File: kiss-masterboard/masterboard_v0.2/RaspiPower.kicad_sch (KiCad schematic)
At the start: 14 parts, among them U1 TPS54327

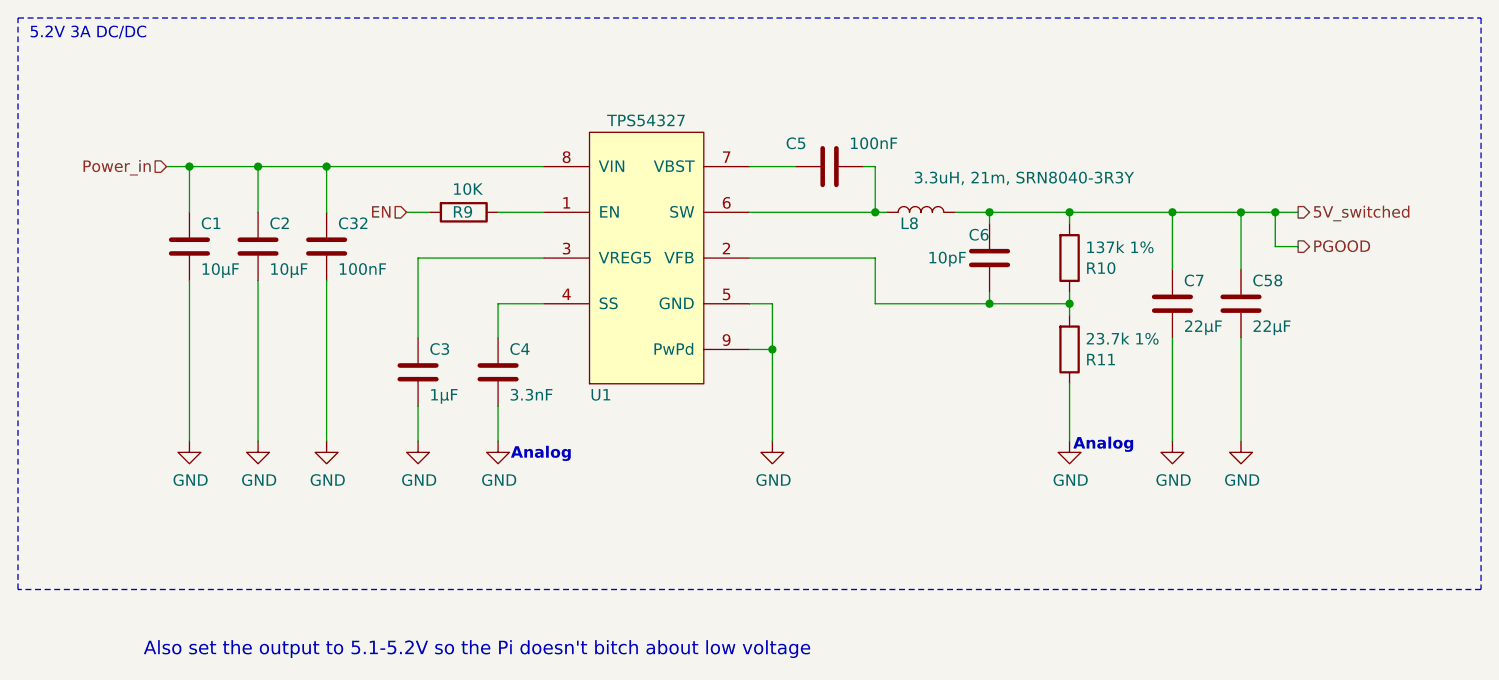
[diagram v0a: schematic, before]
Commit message: Replaced TPS54327 with TPS56339DDC and adjusted the schematic layout accordingly.
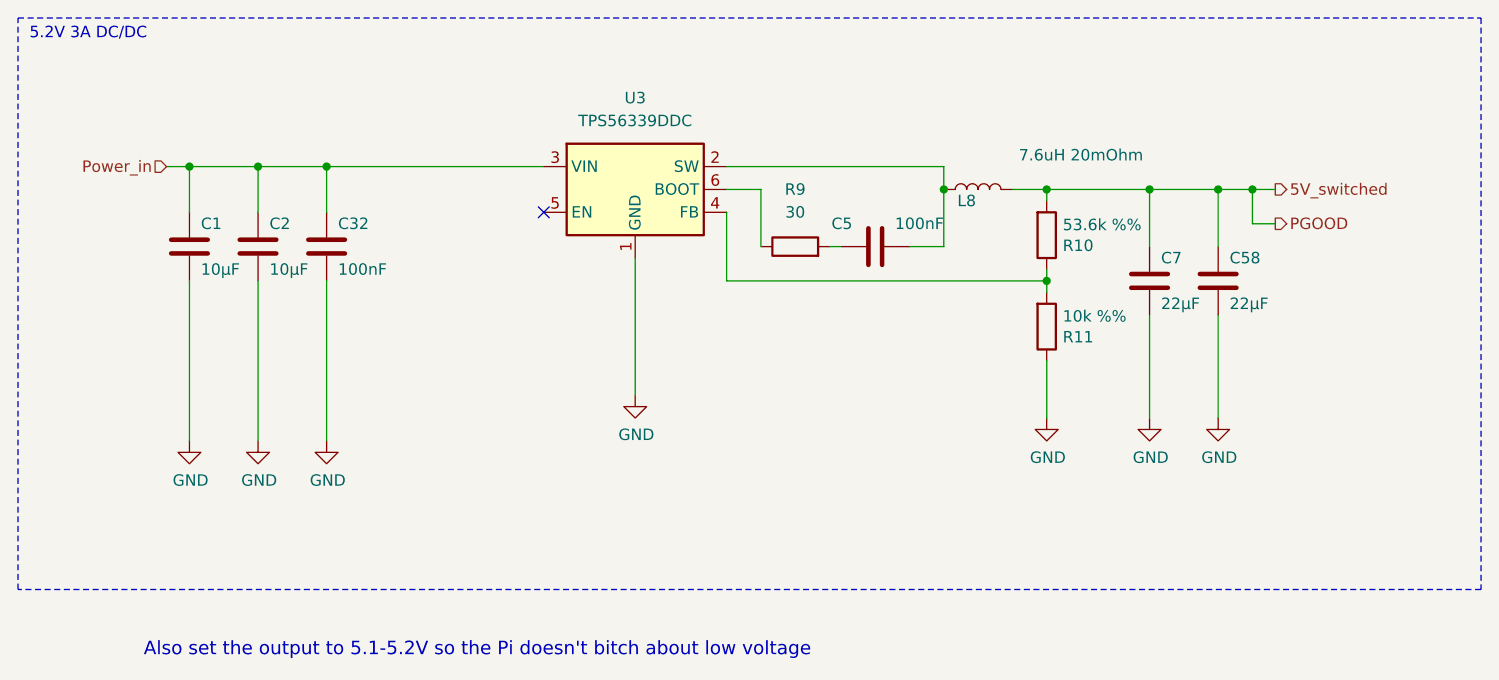
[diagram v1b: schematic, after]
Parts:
- removed C3: 1µF, Capacitor_SMD:C_0603_1608Metric, symbol Device:C
- removed C4: 3.3nF, Capacitor_SMD:C_0603_1608Metric, symbol Device:C
- removed C6: 10pF, Capacitor_SMD:C_0603_1608Metric, symbol Device:C
- removed U1: TPS54327, Package_SO:HSOP-8-1EP_3.9x4.9mm_P1.27mm_EP2.41x3.1mm_ThermalVias, symbol kiss:TPS54327
- added U3: TPS56339DDC, Package_TO_SOT_SMD:SOT-23-6, symbol Regulator_Switching:TPS56339DDC
- L8: value 3.3uH, 21m, SRN8040-3R3Y -> 7.6uH 20mOhm; footprint kiss:Bourns_SRN8040 -> Inductor_SMD:L_12x12mm_H4.5mm
- R10: value 137k 1% -> 53.6k %%
- R11: value 23.7k 1% -> 10k %%
- R9: value 10K -> 30; Digikey No. - -> (none); Manufacturer Yageo -> (none); Package 0603 -> (none); Part No. RC0603JR-0768K -> (none)
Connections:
- net EN is gone; now on an unnamed net: R9.2
- net GND: now also U3.1 (GND)
- net Power_in: now also U3.3 (VIN)
- net at R9.1: now also U3.6 (BOOT)
- net at R10.1, R11.2: now also U3.4 (FB)
- net at C5.2, L8.1: now also U3.2 (SW)
- no-connect marks 0 -> 1
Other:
- note removed: "Analog"
- moved on the sheet: C5, C58, C7, L8, R10, R11

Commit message: Add extension header
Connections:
- net Power_EN: now reaches U3.5 (EN)
- no-connect marks 1 -> 0
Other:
- note added: "CheckEnable Level"
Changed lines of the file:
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@@
+		)
+	)
+	(text "CheckEnable\nLevel"
+		(exclude_from_sim no)
+		(at 73.66 44.196 0)
+		(effects
+			(font
+				(size 3.9878 3.9878)
+			)
 		)
 	)
@@
 		(color 0 0 0 0)
 	)
-	(no_connect
-		(at 73.66 36.83)
-	)
 	(wire
 		(pts
@@
 		(pts
 			(xy 154.94 38.1) (xy 152.4 38.1)
+		)
+		(stroke
+			(width 0)
+			(type default)
+		)
+	)
+	(wire
+		(pts
+			(xy 72.39 36.83) (xy 73.66 36.83)
 		)
 		(stroke
@@
 		(effects
 			(font
+				(size 1.27 1.27)
+			)
+			(justify right)
+		)
+	)
+	(hierarchical_label "Power_EN"
+		(shape input)
+		(at 72.39 36.83 180)
+		(effects
+			(font

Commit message: Added IMU, routed extension layer, switched battery polarity
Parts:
- added R12: 68.8k, Resistor_SMD:R_0603_1608Metric_Pad0.98x0.95mm_HandSolder, symbol Device:R
- added R13: 732k, Resistor_SMD:R_0603_1608Metric_Pad0.98x0.95mm_HandSolder, symbol Device:R
- C1, C2: value 10µF -> 10uF
- C58, C7: value 22µF -> 22uF; footprint Capacitor_SMD:C_1210_3225Metric -> Capacitor_SMD:C_1206_3216Metric
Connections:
- net GND: now also R12.1
- net Power_EN: now also R13.2; no longer U3.5 (EN)
- new net: R12.2, R13.1, U3.5 (EN)
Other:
- note removed: "CheckEnable Level"

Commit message: add cnumbers initial order v04a
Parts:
- C1, C2: JLCNR (none) -> C440198
- C32, C5: JLCNR (none) -> C14663
- C58, C7: JLCNR (none) -> C12891
- L8: JLCNR (none) -> C3040411
- R10: JLCNR (none) -> C2930115
- R11: value 10k %% -> 10K 1%; JLCNR (none) -> C25804
- R12: JLCNR (none) -> C23231
- R13: JLCNR (none) -> C5159703
- R9: JLCNR (none) -> C217958
- U3: JLCNR (none) -> C2071106
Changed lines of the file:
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@@
+			)
+		)
+		(property "JLCNR" "C14663"
+			(at 49.53 40.64 0)
+			(hide yes)
+			(show_name no)
+			(do_not_autoplace no)
+			(effects
+				(font
+					(size 3.9878 3.9878)
+				)
 			)
 		)
@@
 			)
 		)
+		(property "JLCNR" " C440198"
+			(at 34.29 40.64 0)
+			(hide yes)
+			(show_name no)
+			(do_not_autoplace no)
+			(effects
+				(font
+					(size 3.9878 3.9878)
+				)
+			)
+		)
 		(pin "1"
 		)
@@
 			)
 		)
+		(property "JLCNR" "C14663"
+			(at 110.49 40.64 90)
+			(hide yes)
+			(show_name no)
+			(do_not_autoplace no)
+			(effects
+				(font
+					(size 3.9878 3.9878)
+				)
+			)
+		)
 		(pin "1"
 		)
@@
 				(font
 					(size 1.27 1.27)
+				)
+			)
+		)
+		(property "JLCNR" "C3040411"
+			(at 121.92 34.29 90)
+			(hide yes)
+			(show_name no)
+			(do_not_autoplace no)
+			(effects
+				(font
+					(size 3.9878 3.9878)
 				)
 			)
@@
 			)
 		)
+		(property "JLCNR" "C2930115"
+			(at 129.54 39.37 0)
+			(hide yes)
+			(show_name no)
+			(do_not_autoplace no)
+			(effects
+				(font
+					(size 3.9878 3.9878)
+				)
+			)
+		)
 		(pin "1"
 		)
@@
 			)
 		)
-		(property "Value" "10k %%"
+		(property "Value" "10K 1%"
 			(at 131.318 48.387 0)
 			(show_name no)
@@
 				(font
 					(size 1.27 1.27)
+				)
+			)
+		)
+		(property "JLCNR" "C25804"
+			(at 129.54 49.53 0)
+			(hide yes)
+			(show_name no)
+			(do_not_autoplace no)
+			(effects
+				(font
+					(size 3.9878 3.9878)
 				)
 			)
@@
 			)
 		)
+		(property "JLCNR" "C12891"
+			(at 140.97 44.45 0)
+			(hide yes)
+			(show_name no)
+			(do_not_autoplace no)
+			(effects
+				(font
+					(size 3.9878 3.9878)
+				)
+			)
+		)
 		(pin "1"
 		)
@@
 			)
 		)
+		(property "JLCNR" "C12891"
+			(at 148.59 44.45 0)
+			(hide yes)
+			(show_name no)
+			(do_not_autoplace no)
+			(effects
+				(font
+					(size 3.9878 3.9878)
+				)
+			)
+		)
 		(pin "1"
 		)
@@
 			)
 		)
+		(property "JLCNR" " C440198"
+			(at 41.91 40.64 0)
+			(hide yes)
+			(show_name no)
+			(do_not_autoplace no)
+			(effects
+				(font
+					(size 3.9878 3.9878)
+				)
+			)
+		)
 		(pin "1"
 		)
@@
 			)
 		)
+		(property "JLCNR" "C5159703"
+			(at 72.39 44.45 90)
+			(hide yes)
+			(show_name no)
+			(do_not_autoplace no)
+			(effects
+				(font
+					(size 3.9878 3.9878)
+				)
+			)
+		)
 		(pin "1"
 		)
@@
 				(font
 					(size 1.27 1.27)
+				)
+			)
+		)
+		(property "JLCNR" "C23231"
+			(at 68.58 44.45 90)
+			(hide yes)
+			(show_name no)
+			(do_not_autoplace no)
+			(effects
+				(font
+					(size 3.9878 3.9878)
 				)
 			)
@@
 			)
 		)
+		(property "JLCNR" "C217958"
+			(at 101.6 40.64 90)
+			(hide yes)
+			(show_name no)
+			(do_not_autoplace no)
+			(effects
+				(font
+					(size 3.9878 3.9878)
+				)
+			)
+		)
 		(pin "2"
 		)
@@
 				)
 			)
+		)
+		(property "JLCNR" "C2071106"
+			(at 83.82 34.29 0)
+			(hide yes)
+			(show_name no)
+			(do_not_autoplace no)
+			(effects
+				(font
+					(size 3.9878 3.9878)
+				)
+			)
